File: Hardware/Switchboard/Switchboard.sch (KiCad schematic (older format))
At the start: 50 parts, among them J1 S88_In_Header, J2 S88_In_Plug, J3 S88_Out_Header, J4 S88_Out_Plug, Q1 BC237, SW1 SW_Push, SW2 SW_Push, SW3 SW_Push, SW4 SW_Push, SW5 SW_Push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

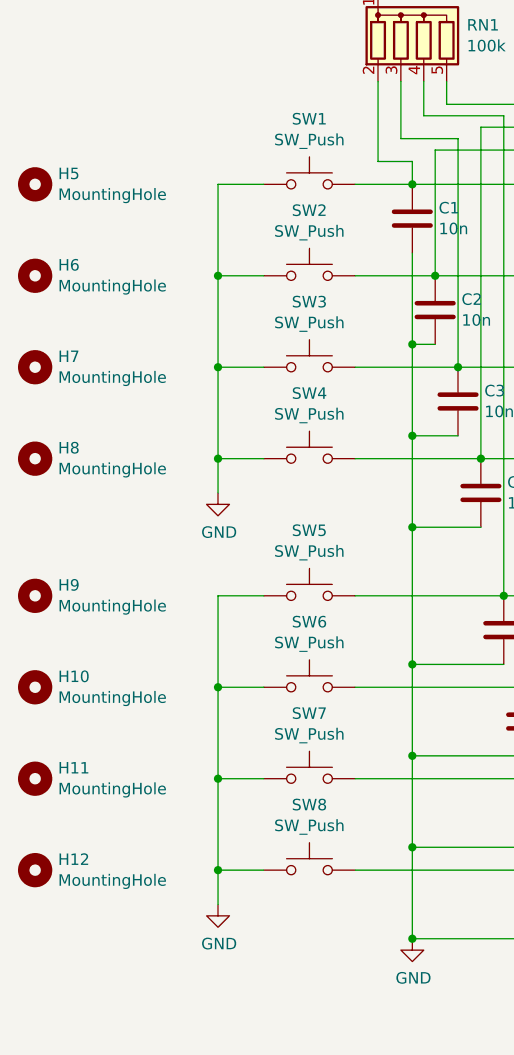
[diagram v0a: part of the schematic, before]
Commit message: Converted mounting holes to vias
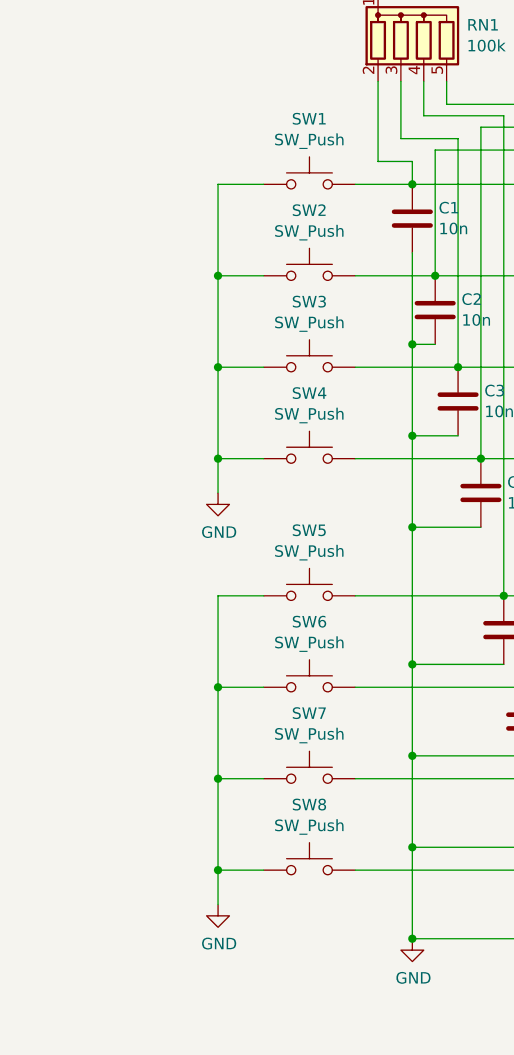
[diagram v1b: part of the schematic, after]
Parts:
- removed H10, H11, H12, H5, H6, H7, H8, H9: MountingHole, MountingHole:MountingHole_2.1mm, symbol Mechanical:MountingHole
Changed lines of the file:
@@
 	7850 3800 8250 3800
-$Comp
-L Mechanical:MountingHole H5
-U 1 1 5E2908DC
-P 1000 1600
-F 0 "H5" H 1100 1646 50  0000 L CNN
-F 1 "MountingHole" H 1100 1555 50  0000 L CNN
-F 2 "MountingHole:MountingHole_2.1mm" H 1000 1600 50  0001 C CNN
-F 3 "~" H 1000 1600 50  0001 C CNN
-	1    1000 1600
-	1    0    0    -1
-$EndComp
-$Comp
-L Mechanical:MountingHole H6
-U 1 1 5E291344
-P 1000 2000
-F 0 "H6" H 1100 2046 50  0000 L CNN
-F 1 "MountingHole" H 1100 1955 50  0000 L CNN
-F 2 "MountingHole:MountingHole_2.1mm" H 1000 2000 50  0001 C CNN
-F 3 "~" H 1000 2000 50  0001 C CNN
-	1    1000 2000
-	1    0    0    -1
-$EndComp
-$Comp
-L Mechanical:MountingHole H7
-U 1 1 5E291646
-P 1000 2400
-F 0 "H7" H 1100 2446 50  0000 L CNN
-F 1 "MountingHole" H 1100 2355 50  0000 L CNN
-F 2 "MountingHole:MountingHole_2.1mm" H 1000 2400 50  0001 C CNN
-F 3 "~" H 1000 2400 50  0001 C CNN
-	1    1000 2400
-	1    0    0    -1
-$EndComp
-$Comp
-L Mechanical:MountingHole H8
-U 1 1 5E291650
-P 1000 2800
-F 0 "H8" H 1100 2846 50  0000 L CNN
-F 1 "MountingHole" H 1100 2755 50  0000 L CNN
-F 2 "MountingHole:MountingHole_2.1mm" H 1000 2800 50  0001 C CNN
-F 3 "~" H 1000 2800 50  0001 C CNN
-	1    1000 2800
-	1    0    0    -1
-$EndComp
-$Comp
-L Mechanical:MountingHole H9
-U 1 1 5E29E708
-P 1000 3400
-F 0 "H9" H 1100 3446 50  0000 L CNN
-F 1 "MountingHole" H 1100 3355 50  0000 L CNN
-F 2 "MountingHole:MountingHole_2.1mm" H 1000 3400 50  0001 C CNN
-F 3 "~" H 1000 3400 50  0001 C CNN
-	1    1000 3400
-	1    0    0    -1
-$EndComp
-$Comp
-L Mechanical:MountingHole H10
-U 1 1 5E29E712
-P 1000 3800
-F 0 "H10" H 1100 3846 50  0000 L CNN
-F 1 "MountingHole" H 1100 3755 50  0000 L CNN
-F 2 "MountingHole:MountingHole_2.1mm" H 1000 3800 50  0001 C CNN
-F 3 "~" H 1000 3800 50  0001 C CNN
-	1    1000 3800
-	1    0    0    -1
-$EndComp
-$Comp
-L Mechanical:MountingHole H11
-U 1 1 5E29E71C
-P 1000 4200
-F 0 "H11" H 1100 4246 50  0000 L CNN
-F 1 "MountingHole" H 1100 4155 50  0000 L CNN
-F 2 "MountingHole:MountingHole_2.1mm" H 1000 4200 50  0001 C CNN
-F 3 "~" H 1000 4200 50  0001 C CNN
-	1    1000 4200
-	1    0    0    -1
-$EndComp
-$Comp
-L Mechanical:MountingHole H12
-U 1 1 5E29E726
-P 1000 4600
-F 0 "H12" H 1100 4646 50  0000 L CNN
-F 1 "MountingHole" H 1100 4555 50  0000 L CNN
-F 2 "MountingHole:MountingHole_2.1mm" H 1000 4600 50  0001 C CNN
-F 3 "~" H 1000 4600 50  0001 C CNN
-	1    1000 4600
-	1    0    0    -1
-$EndComp
 $Comp
 L Device:R_Network04 RN1
